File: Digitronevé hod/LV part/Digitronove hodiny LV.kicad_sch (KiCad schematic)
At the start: 82 parts, among them J1 DD4012SA, J10 Output, J11 Output, J12 Output, J14 9V to 170V, J15 Output, J16 Output, J19 Output, J20 Output, J21 Output, J22 Output, J23 Output, J24 RCWL-0516, J25 Output, J26 Output, J27 Output, J28 Output, J29 Output, J3 Output, J30 Output, J31 Output, J32 Output, J33 Output, J39 Output, J4 Output, J40 Output, J41 Output, J43 Output, J5 Output, J6 Output, J7 Output, J8 Output, J9 Output, SW1 RESET, SW2 START/STOP, SW3 +1, SW4 SWITCH, U1 74HC595, U2 74HC595, U4 74HC595, U5 74HC595, U6 74HC595, U7 74HC595

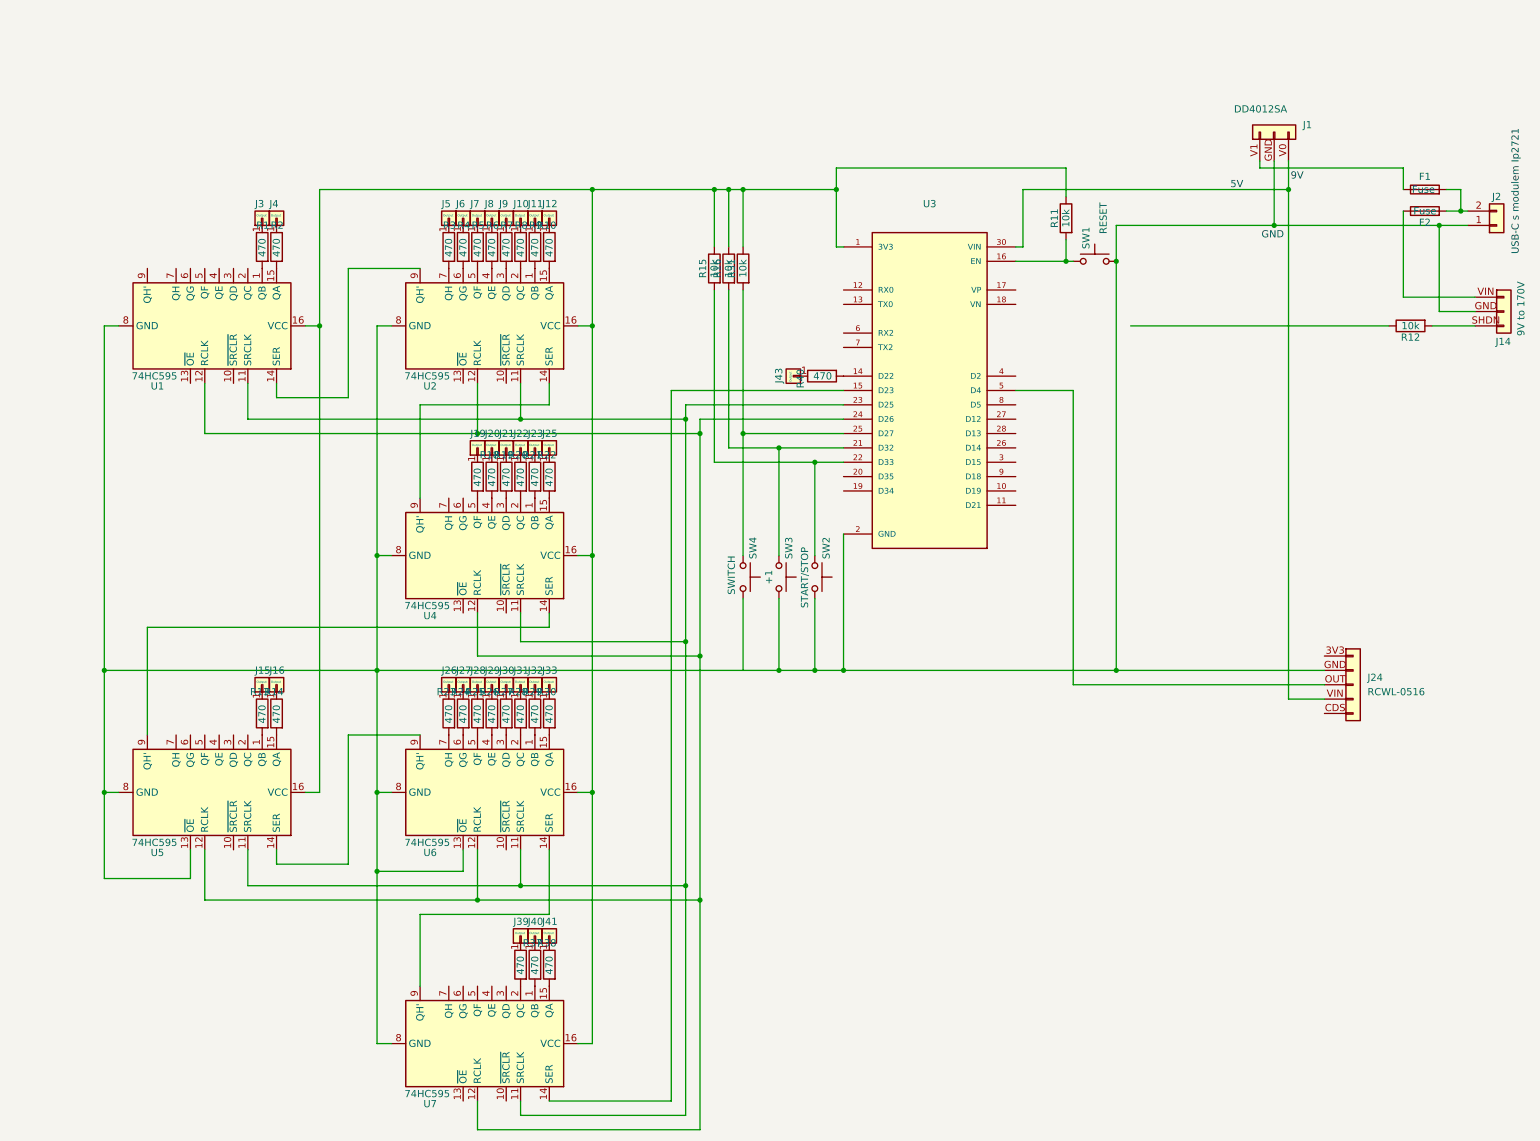
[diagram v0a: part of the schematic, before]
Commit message: PCB LV upravování pouzder
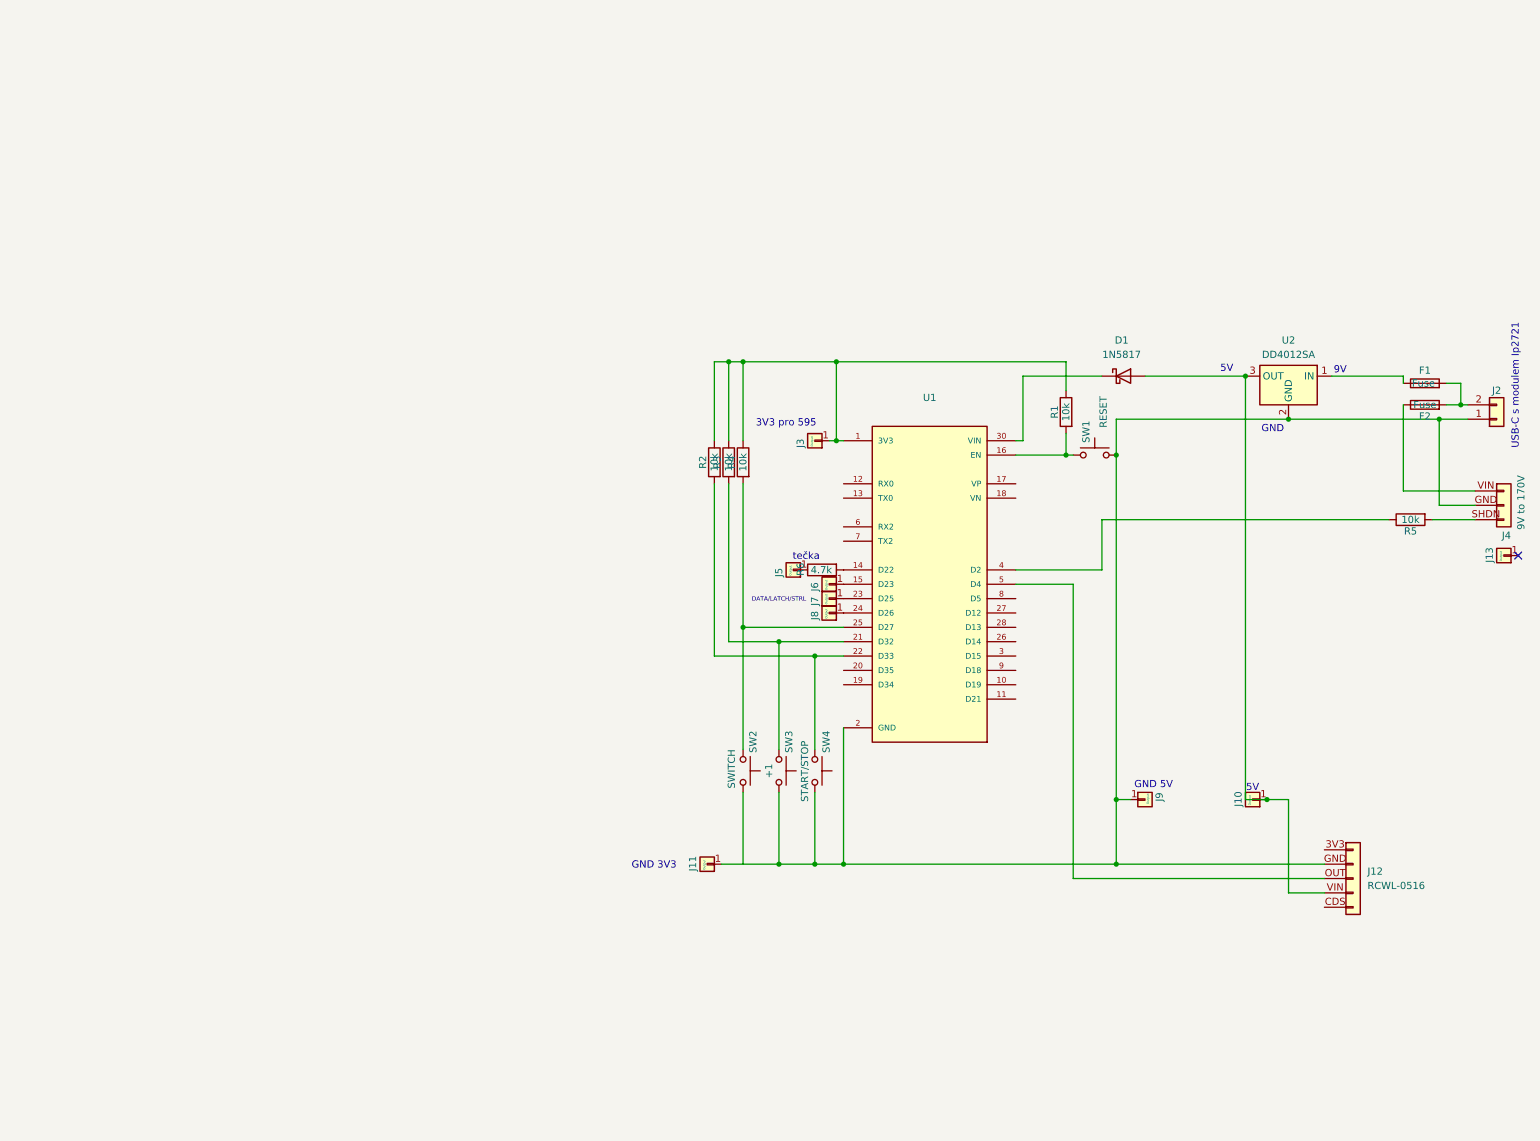
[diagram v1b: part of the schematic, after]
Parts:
- removed J1: DD4012SA, Converter_DCDC:Converter_DCDC_RECOM_R-78HB-0.5L_THT, symbol Connector_Generic:Conn_01x03
- removed J12, J15, J16, J19, J20, J21, J22, J23, J25, J26, J27, J28, J29, J30, J31, J32, J33, J39, J4, J40, J41, J5: Output, Connector_PinHeader_1.00mm:PinHeader_1x01_P1.00mm_Horizontal, symbol Connector_Generic:Conn_01x01
- removed R1, R10, R13, R14, R17, R18, R19, R2, R20, R21, R22, R23, R24, R25, R26, R27, R28, R29, R3, R30, R36, R37, R38, R4, R5, R6, R7, R8, R9: 470, Resistor_SMD:R_1206_3216Metric_Pad1.30x1.75mm_HandSolder, symbol Device:R
- removed U1, U2, U4, U5, U6, U7: 74HC595, LOGIC-74HC595N_DIP16_:74HC595N, symbol 74xx:74HC595
- added D1: 1N5817, Diode_THT:D_DO-41_SOD81_P10.16mm_Horizontal, symbol Diode:1N5817
- added J13: Output, LOGIC-74HC595N_DIP16_:MAX1771, symbol Connector_Generic:Conn_01x01
- added U2: DD4012SA, Converter_DCDC:Converter_DCDC_Murata_OKI-78SR_Horizontal, symbol Converter_DCDC:OKI-78SR-5_1.5-W36H-C
- F1, F2: footprint Fuse:Fuse_1812_4532Metric -> Fuse:Fuseholder_Cylinder-5x20mm_Stelvio-Kontek_PTF78_Horizontal_Open
- R1: renamed from R11; footprint Resistor_SMD:R_1206_3216Metric_Pad1.30x1.75mm_HandSolder -> Resistor_THT:R_Axial_DIN0207_L6.3mm_D2.5mm_P10.16mm_Horizontal
- R2: renamed from R15; footprint Resistor_SMD:R_1206_3216Metric_Pad1.30x1.75mm_HandSolder -> Resistor_THT:R_Axial_DIN0207_L6.3mm_D2.5mm_P10.16mm_Horizontal
- R3: renamed from R16; footprint Resistor_SMD:R_1206_3216Metric_Pad1.30x1.75mm_HandSolder -> Resistor_THT:R_Axial_DIN0207_L6.3mm_D2.5mm_P10.16mm_Horizontal
- R4: renamed from R31; footprint Resistor_SMD:R_1206_3216Metric_Pad1.30x1.75mm_HandSolder -> Resistor_THT:R_Axial_DIN0207_L6.3mm_D2.5mm_P10.16mm_Horizontal
- R5: renamed from R12; footprint Resistor_SMD:R_1206_3216Metric_Pad1.30x1.75mm_HandSolder -> Resistor_THT:R_Axial_DIN0207_L6.3mm_D2.5mm_P10.16mm_Horizontal
- R6: renamed from R40; value 470 -> 4.7k; footprint Resistor_SMD:R_1206_3216Metric_Pad1.30x1.75mm_HandSolder -> Resistor_THT:R_Axial_DIN0207_L6.3mm_D2.5mm_P10.16mm_Horizontal
- U1: renamed from U3; footprint ESP32-DEVKIT-V1:MODULE_ESP32_DEVKIT_V1 -> LOGIC-74HC595N_DIP16_:MODULE_ESP32_DEVKIT_V1
- renumbered J24 to J12, J14 to J4, J43 to J5, SW4 to SW2, SW2 to SW4
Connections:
- net GND: now also J11.1 (Pin_1), J9.1 (Pin_1), U2.2 (GND)
- net at J10.1 (Pin_1): now also J12.VIN (Pin_4), D1.2 (A), U2.3 (OUT)
- net at U1.23 (D25): now also J7.1 (Pin_1)
- net at U1.24 (D26): now also J8.1 (Pin_1)
- net at R1.1, R2.1, R3.1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: now also J3.1 (Pin_1)
- net at U1.30 (VIN): now also D1.1 (K); no longer J12.VIN (Pin_4)
- net at J6.1 (Pin_1): now also U1.15 (D23)
- net at R5.1: now also U1.4 (D2)
- net at F1.1: now also U2.1 (IN)
- no-connect marks 2 -> 3
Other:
- note added: "3V3 pro 595"
- note added: "DATA/LATCH/STRL"
- note added: "GND 3V3"
- note added: "GND 5V"
- note added: "tečka"
- moved on the sheet: F1, F2, J12, J2, J4, J5, R1, R2, R3, R4, R5, R6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

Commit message: Update Schéma LV
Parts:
- removed J13: Output, LOGIC-74HC595N_DIP16_:MAX1771, symbol Connector_Generic:Conn_01x01
- removed J4: 9V to 170V, Connector_PinHeader_1.00mm:PinHeader_1x03_P1.00mm_Horizontal, symbol Connector_Generic:Conn_01x03
- added J3: MAX1771 module, LOGIC-74HC595N_DIP16_:MAX1771, symbol Connector_Generic:Conn_01x03
- F1, F2: footprint Fuse:Fuseholder_Cylinder-5x20mm_Stelvio-Kontek_PTF78_Horizontal_Open -> Fuse:Fuse_1812_4532Metric
- J10: renamed from J9; value Output -> GND; footprint Connector_PinHeader_1.00mm:PinHeader_1x01_P1.00mm_Horizontal -> Connector_PinHeader_1.00mm:PinHeader_1x01_P1.00mm_Vertical
- J11: renamed from J10; value Output -> 5V; footprint Connector_PinHeader_1.00mm:PinHeader_1x01_P1.00mm_Horizontal -> Connector_PinHeader_1.00mm:PinHeader_1x01_P1.00mm_Vertical
- J12: renamed from J11; value Output -> GND; footprint Connector_PinHeader_1.00mm:PinHeader_1x01_P1.00mm_Horizontal -> Connector_PinHeader_1.00mm:PinHeader_1x01_P1.00mm_Vertical
- J2: renamed from J3; value Output -> 3V3; footprint Connector_PinHeader_1.00mm:PinHeader_1x01_P1.00mm_Horizontal -> Connector_PinHeader_1.00mm:PinHeader_1x01_P1.00mm_Vertical
- J6: renamed from J5; footprint Connector_PinHeader_1.00mm:PinHeader_1x01_P1.00mm_Horizontal -> Connector_PinHeader_1.00mm:PinHeader_1x01_P1.00mm_Vertical
- J7: renamed from J6; value Output -> DATA; footprint Connector_PinHeader_1.00mm:PinHeader_1x01_P1.00mm_Horizontal -> Connector_PinHeader_1.00mm:PinHeader_1x01_P1.00mm_Vertical
- J8: renamed from J7; value Output -> LATCH; footprint Connector_PinHeader_1.00mm:PinHeader_1x01_P1.00mm_Horizontal -> Connector_PinHeader_1.00mm:PinHeader_1x01_P1.00mm_Vertical
- J9: renamed from J8; value Output -> STRL; footprint Connector_PinHeader_1.00mm:PinHeader_1x01_P1.00mm_Horizontal -> Connector_PinHeader_1.00mm:PinHeader_1x01_P1.00mm_Vertical
- U1: renamed from U2; footprint Converter_DCDC:Converter_DCDC_Murata_OKI-78SR_Horizontal -> LOGIC-74HC595N_DIP16_:Untitled_3
- renumbered J2 to J1, J12 to J13, U1 to U2
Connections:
- net GND: now also J1.2 (Pin_2), SW2.1, J3.GND (Pin_2); no longer J1.1 (Pin_1)
- net 5V: now reaches D1.2 (A), J11.1 (Pin_1), J13.VIN (Pin_4), U1.3 (OUT)
- net 5V: now also D1.1 (K), U2.30 (VIN)
- net 9V: now reaches F2.1
- net 9V: now also F1.1, F1.2, F2.2, J1.1 (Pin_1), U1.1 (IN), J3.VIN (Pin_1)
- net SHDN: now reaches R5.2
- net SHDN: now also R5.1, U2.4 (D2), J3.SHDN (Pin_3)
- net 3V3: now reaches R4.2, SW2.2, U2.25 (D27)
- net 3V3: now also J2.1 (Pin_1), R1.1, R2.1, R2.2, R3.1, R3.2, R4.1, SW3.2, SW4.2, U2.1 (3V3), U2.21 (D32), U2.22 (D33)
- net EN: now reaches R1.2, SW1.2, U2.16 (EN)
- no-connect marks 3 -> 2
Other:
- note removed: "GND 3V3"
- note removed: "GND 5V"
- moved on the sheet: J1, J11, SW1

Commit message: Dokončení LV
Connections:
- net 3V3: no longer R2.2, R3.2, R4.2, SW2.2, SW3.2, SW4.2, U2.21 (D32), U2.22 (D33), U2.25 (D27)
- new net +1: R3.2, SW3.2, U2.21 (D32)
- new net START/STOP: R2.2, SW4.2, U2.22 (D33)
- new net SWITCH: R4.2, SW2.2, U2.25 (D27)
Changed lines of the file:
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@@
+		)
+	)
+	(label "SWITCH"
+		(at 147.32 104.14 0)
+		(effects
+			(font
+				(size 1.27 1.27)
+			)
+			(justify left bottom)
 		)
 	)
@@
 	)
 	(label "3V3"
-		(at 139.7 90.17 0)
+		(at 156.21 63.5 0)
 		(effects
 			(font
@@
 		)
 	)
-	(label "3V3"
-		(at 156.21 63.5 0)
+	(label "+1"
+		(at 148.59 106.68 0)
 		(effects
 			(font
@@
 		)
 	)
-	(label "3V3"
-		(at 134.62 91.0986 0)
-		(effects
-			(font
-				(size 1.27 1.27)
-			)
-			(justify left bottom)
-		)
-	)
 	(label "9V"
 		(at 256.54 78.74 0)
@@
 		)
 	)
-	(label "3V3"
-		(at 137.16 90.678 0)
+	(label "START{slash}STOP"
+		(at 154.94 109.22 0)
 		(effects
 			(font

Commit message: LV update
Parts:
- removed R2, R3: 10k, Resistor_THT:R_Axial_DIN0207_L6.3mm_D2.5mm_P10.16mm_Horizontal, symbol Device:R
- added R5, R6: 10k, Resistor_THT:R_Axial_DIN0207_L6.3mm_D2.5mm_P10.16mm_Horizontal, symbol Device:R
- renumbered J12 to J10, J13 to J11, J6 to J4, J7 to J5, J8 to J6, J9 to J7, J10 to J8, J11 to J9, R5 to R2, R6 to R3
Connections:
- net +1: now also SW3.1, R5.1; no longer SW3.2
- net 3V3: now also SW1.1, SW2.2, SW3.2, SW4.2; no longer R1.1, R4.1
- net EN: now also R1.1; no longer R1.2
- net GND: now also R1.2, R4.2, R5.2, R6.2; no longer SW1.1, SW2.1, SW3.1, SW4.1
- net START/STOP: now also SW2.1, R6.1; no longer SW4.2
- net SWITCH: now also R4.1, SW4.1; no longer R4.2, SW2.2
